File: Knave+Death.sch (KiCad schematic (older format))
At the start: 42 parts, among them J1 OUT0_3.5mm, J2 OUT1_3.5mm, J3 OUT2_3.5mm, J4 PWR_IN_PHNX, J5 OUT3_3.5mm, J6 E0_3.5mm, J7 E1_3.5mm, SW1 SW_SPDT, U1 LM324, U2 LM358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

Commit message: commit before changing schematic
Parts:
- added J8: E1_3.5mm, HammerheadAudio:EuroJack_MonoSW_THT, symbol Connector:Conn_01x03_Male
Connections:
- net GND: now also J8.2 (Pin_2)
- net at U4.14 (CLK): now also J8.1 (Pin_1); no longer U5.3 (Q)
- new net: J8.3 (Pin_3), U5.3 (Q)
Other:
- moved on the sheet: C2, R14, R15, RV1, U5
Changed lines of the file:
@@
 L Timer:NE555 U5
 U 1 1 5E794E13
-P 5100 5300
-F 0 "U5" H 4800 5650 50  0000 C CNN
-F 1 "NE555" H 5350 5650 50  0000 C CNN
-F 2 "Package_DIP:DIP-8_W7.62mm_Socket" H 5100 5300 50  0001 C CNN
-F 3 "http://www.ti.com/lit/ds/symlink/ne555.pdf" H 5100 5300 50  0001 C CNN
-	1    5100 5300
-	1    0    0    -1
-$EndComp
-Wire Wire Line
-	5600 5100 6400 5100
+P 4600 5300
+F 0 "U5" H 4300 5650 50  0000 C CNN
+F 1 "NE555" H 4850 5650 50  0000 C CNN
+F 2 "Package_DIP:DIP-8_W7.62mm_Socket" H 4600 5300 50  0001 C CNN
+F 3 "http://www.ti.com/lit/ds/symlink/ne555.pdf" H 4600 5300 50  0001 C CNN
+	1    4600 5300
+	1    0    0    -1
+$EndComp
 $Comp
 L power:VCC #PWR026
 U 1 1 5E7974FB
-P 4400 5500
-F 0 "#PWR026" H 4400 5350 50  0001 C CNN
-F 1 "VCC" H 4417 5673 50  0000 C CNN
-F 2 "" H 4400 5500 50  0001 C CNN
-F 3 "" H 4400 5500 50  0001 C CNN
-	1    4400 5500
-	1    0    0    -1
-$EndComp
-NoConn ~ 4600 5300
-Wire Wire Line
-	4600 5500 4400 5500
+P 3900 5500
+F 0 "#PWR026" H 3900 5350 50  0001 C CNN
+F 1 "VCC" H 3917 5673 50  0000 C CNN
+F 2 "" H 3900 5500 50  0001 C CNN
+F 3 "" H 3900 5500 50  0001 C CNN
+	1    3900 5500
+	1    0    0    -1
+$EndComp
+NoConn ~ 4100 5300
+Wire Wire Line
+	4100 5500 3900 5500
 $Comp
 L power:GND #PWR028
 U 1 1 5E798069
-P 5100 5750
-F 0 "#PWR028" H 5100 5500 50  0001 C CNN
-F 1 "GND" H 5105 5577 50  0000 C CNN
-F 2 "" H 5100 5750 50  0001 C CNN
-F 3 "" H 5100 5750 50  0001 C CNN
-	1    5100 5750
-	1    0    0    -1
-$EndComp
-Wire Wire Line
-	5100 5750 5100 5700
+P 4600 5750
+F 0 "#PWR028" H 4600 5500 50  0001 C CNN
+F 1 "GND" H 4605 5577 50  0000 C CNN
+F 2 "" H 4600 5750 50  0001 C CNN
+F 3 "" H 4600 5750 50  0001 C CNN
+	1    4600 5750
+	1    0    0    -1
+$EndComp
+Wire Wire Line
+	4600 5750 4600 5700
 $Comp
 L Device:R R15
 U 1 1 5E7988F4
-P 5800 5500
-F 0 "R15" H 5870 5546 50  0000 L CNN
-F 1 "1k" H 5870 5455 50  0000 L CNN
-F 2 "HammerheadAudio:R_THT_P7.62" V 5730 5500 50  0001 C CNN
-F 3 "~" H 5800 5500 50  0001 C CNN
-	1    5800 5500
+P 5300 5500
+F 0 "R15" H 5370 5546 50  0000 L CNN
+F 1 "1k" H 5370 5455 50  0000 L CNN
+F 2 "HammerheadAudio:R_THT_P7.62" V 5230 5500 50  0001 C CNN
+F 3 "~" H 5300 5500 50  0001 C CNN
+	1    5300 5500
 	-1   0    0    1
 $EndComp
@@
 L Device:R R14
 U 1 1 5E799458
-P 5800 4850
-F 0 "R14" H 5870 4896 50  0000 L CNN
-F 1 "1k" H 5870 4805 50  0000 L CNN
-F 2 "HammerheadAudio:R_THT_P7.62" V 5730 4850 50  0001 C CNN
-F 3 "~" H 5800 4850 50  0001 C CNN
-	1    5800 4850
+P 5300 4850
+F 0 "R14" H 5370 4896 50  0000 L CNN
+F 1 "1k" H 5370 4805 50  0000 L CNN
+F 2 "HammerheadAudio:R_THT_P7.62" V 5230 4850 50  0001 C CNN
+F 3 "~" H 5300 4850 50  0001 C CNN
+	1    5300 4850
 	-1   0    0    1
 $EndComp
 Wire Wire Line
-	5800 5350 5800 5300
-Wire Wire Line
-	5800 5000 5800 5300
-Connection ~ 5800 5300
-Wire Wire Line
-	5100 4900 5100 4650
+	5300 5350 5300 5300
+Wire Wire Line
+	5300 5000 5300 5300
+Connection ~ 5300 5300
+Wire Wire Line
+	4600 4900 4600 4650
 $Comp
 L power:VCC #PWR022
 U 1 1 5E79A9DD
-P 5100 4600
-F 0 "#PWR022" H 5100 4450 50  0001 C CNN
-F 1 "VCC" H 5117 4773 50  0000 C CNN
-F 2 "" H 5100 4600 50  0001 C CNN
-F 3 "" H 5100 4600 50  0001 C CNN
-	1    5100 4600
-	1    0    0    -1
-$EndComp
-Wire Wire Line
-	5100 4650 5100 4600
-Connection ~ 5100 4650
+P 4600 4600
+F 0 "#PWR022" H 4600 4450 50  0001 C CNN
+F 1 "VCC" H 4617 4773 50  0000 C CNN
+F 2 "" H 4600 4600 50  0001 C CNN
+F 3 "" H 4600 4600 50  0001 C CNN
+	1    4600 4600
+	1    0    0    -1
+$EndComp
+Wire Wire Line
+	4600 4650 4600 4600
+Connection ~ 4600 4650
 $Comp
 L Device:R_POT_TRIM RV1
 U 1 1 5E79B5EB
-P 5800 5850
-F 0 "RV1" H 5730 5804 50  0000 R CNN
-F 1 "1M" H 5730 5895 50  0000 R CNN
-F 2 "Potentiometer_THT:Potentiometer_Piher_PT-6-V_Vertical" H 5800 5850 50  0001 C CNN
-F 3 "~" H 5800 5850 50  0001 C CNN
-	1    5800 5850
+P 5300 5850
+F 0 "RV1" H 5230 5804 50  0000 R CNN
+F 1 "1M" H 5230 5895 50  0000 R CNN
+F 2 "Potentiometer_THT:Potentiometer_Piher_PT-6-V_Vertical" H 5300 5850 50  0001 C CNN
+F 3 "~" H 5300 5850 50  0001 C CNN
+	1    5300 5850
 	-1   0    0    1
 $EndComp
 Wire Wire Line
-	5800 5700 5800 5650
-Wire Wire Line
-	5800 4650 5800 4700
-Wire Wire Line
-	5100 4650 5800 4650
-Wire Wire Line
-	5600 5300 5800 5300
-Wire Wire Line
-	5600 5500 5600 5850
-Wire Wire Line
-	5600 6050 4300 6050
-Wire Wire Line
-	4300 6050 4300 5100
-Wire Wire Line
-	4300 5100 4600 5100
-Wire Wire Line
-	5600 5850 5650 5850
-Connection ~ 5600 5850
-Wire Wire Line
-	5600 5850 5600 6050
-Wire Wire Line
-	5800 6000 5800 6050
-Wire Wire Line
-	5800 6050 5600 6050
-Connection ~ 5600 6050
+	5300 5700 5300 5650
+Wire Wire Line
+	5300 4650 5300 4700
+Wire Wire Line
+	4600 4650 5300 4650
+Wire Wire Line
+	5100 5300 5300 5300
+Wire Wire Line
+	5100 5500 5100 5850
+Wire Wire Line
+	5100 6050 3800 6050
+Wire Wire Line
+	3800 6050 3800 5100
+Wire Wire Line
+	3800 5100 4100 5100
+Wire Wire Line
+	5100 5850 5150 5850
+Connection ~ 5100 5850
+Wire Wire Line
+	5100 5850 5100 6050
+Wire Wire Line
+	5300 6000 5300 6050
+Wire Wire Line
+	5300 6050 5100 6050
+Connection ~ 5100 6050
 NoConn ~ 7200 5100
 NoConn ~ 7200 5200
@@
 L Device:CP C2
 U 1 1 5E7A1F2F
-P 4300 6250
-F 0 "C2" H 4418 6296 50  0000 L CNN
-F 1 "CP" H 4418 6205 50  0000 L CNN
-F 2 "Capacitor_THT:CP_Radial_D6.3mm_P2.50mm" H 4338 6100 50  0001 C CNN
-F 3 "~" H 4300 6250 50  0001 C CNN
-	1    4300 6250
+P 3800 6250
+F 0 "C2" H 3918 6296 50  0000 L CNN
+F 1 "CP" H 3918 6205 50  0000 L CNN
+F 2 "Capacitor_THT:CP_Radial_D6.3mm_P2.50mm" H 3838 6100 50  0001 C CNN
+F 3 "~" H 3800 6250 50  0001 C CNN
+	1    3800 6250
 	1    0    0    -1
 $EndComp
@@
 L power:GND #PWR029
 U 1 1 5E7A2621
-P 4300 6450
-F 0 "#PWR029" H 4300 6200 50  0001 C CNN
-F 1 "GND" H 4305 6277 50  0000 C CNN
-F 2 "" H 4300 6450 50  0001 C CNN
-F 3 "" H 4300 6450 50  0001 C CNN
-	1    4300 6450
-	1    0    0    -1
-$EndComp
-Wire Wire Line
-	4300 6100 4300 6050
-Connection ~ 4300 6050
-Wire Wire Line
-	4300 6450 4300 6400
+P 3800 6450
+F 0 "#PWR029" H 3800 6200 50  0001 C CNN
+F 1 "GND" H 3805 6277 50  0000 C CNN
+F 2 "" H 3800 6450 50  0001 C CNN
+F 3 "" H 3800 6450 50  0001 C CNN
+	1    3800 6450
+	1    0    0    -1
+$EndComp
+Wire Wire Line
+	3800 6100 3800 6050
+Connection ~ 3800 6050
+Wire Wire Line
+	3800 6450 3800 6400
 $Comp
 L SparkFun-IC-Logic:CD4017 U3
@@
 Wire Wire Line
 	8500 5050 8550 5050
+$Comp
+L Connector:Conn_01x03_Male J8
+U 1 1 5E7ABC41
+P 6050 4450
+F 0 "J8" H 6158 4731 50  0000 C CNN
+F 1 "E1_3.5mm" H 6158 4640 50  0000 C CNN
+F 2 "HammerheadAudio:EuroJack_MonoSW_THT" H 6050 4450 50  0001 C CNN
+F 3 "~" H 6050 4450 50  0001 C CNN
+	1    6050 4450
+	0    1    1    0
+$EndComp
+Wire Wire Line
+	6050 4650 6050 4750
+$Comp
+L power:GND #PWR0101
+U 1 1 5E7ABC4D
+P 6050 4750
+F 0 "#PWR0101" H 6050 4500 50  0001 C CNN
+F 1 "GND" V 6055 4622 50  0000 R CNN
+F 2 "" H 6050 4750 50  0001 C CNN
+F 3 "" H 6050 4750 50  0001 C CNN
+	1    6050 4750
+	1    0    0    -1
+$EndComp
+Wire Wire Line
+	6150 4650 6150 5100
+Wire Wire Line
+	6150 5100 6400 5100
+Wire Wire Line
+	5950 4650 5950 5100
+Wire Wire Line
+	5100 5100 5950 5100
 $EndSCHEMATC

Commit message: updated schematic
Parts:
- added C3: 10uf, Capacitor_THT:CP_Radial_D6.3mm_P2.50mm, symbol Device:CP
- added D9: LED, LED_THT:LED_D5.0mm, symbol Device:LED
- added R16, R18, R19: 1k, HammerheadAudio:R_THT_P7.62, symbol Device:R
- added R17: 220, HammerheadAudio:R_THT_P7.62, symbol Device:R
- added unit 3 of U2
- added unit 4 of U2
- C2: value CP -> 10uf
- R10, R12, R14, R15, R2, R4, R6, R8: value 1k -> 220
- RV1: value 1M -> 100k
- U2: value LM358 -> LM324; footprint Package_DIP:DIP-8_W7.62mm_Socket -> Package_DIP:DIP-14_W7.62mm_Socket; symbol Amplifier_Operational:LM358 -> Amplifier_Operational:LM324
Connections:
- net GND: now also U2.11 (V-), C3.2, D9.1 (K), R19.1; no longer U2.4 (V-)
- net OUT0: no longer U1.2 (-)
- net VCC: now also U2.4 (V+), R18.2; no longer U2.8 (V+)
- net TRIG_IN: now reaches J8.1 (Pin_1)
- net TRIG_IN: now also U2.10 (+); no longer U4.14 (CLK)
- net at C2.1, RV1.1, RV1.2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: now also C3.1
- net at R3.2, R4.2, U1.7: no longer U1.6 (-)
- net at R7.2, R8.2, U1.14: no longer U1.13 (-)
- net at R10.2, R9.2, U2.1: no longer U2.2 (-)
- net at R11.2, R12.2, U2.7: no longer U2.6 (-)
- new net: R16.2, R17.2, U2.8
- new net: D9.2 (A), R17.1
- new net: R18.1, R19.2, U2.12 (+)
- new net TRIG_OUT: R16.1, U4.14 (CLK)
- new net VREF: U1.13 (-), U1.2 (-), U1.6 (-), U2.13 (-), U2.14, U2.2 (-), U2.6 (-), U2.9 (-)
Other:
- moved on the sheet: D0, D1, D2, D3, D4, D5, J1, J2, J3, J5, J6, J7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

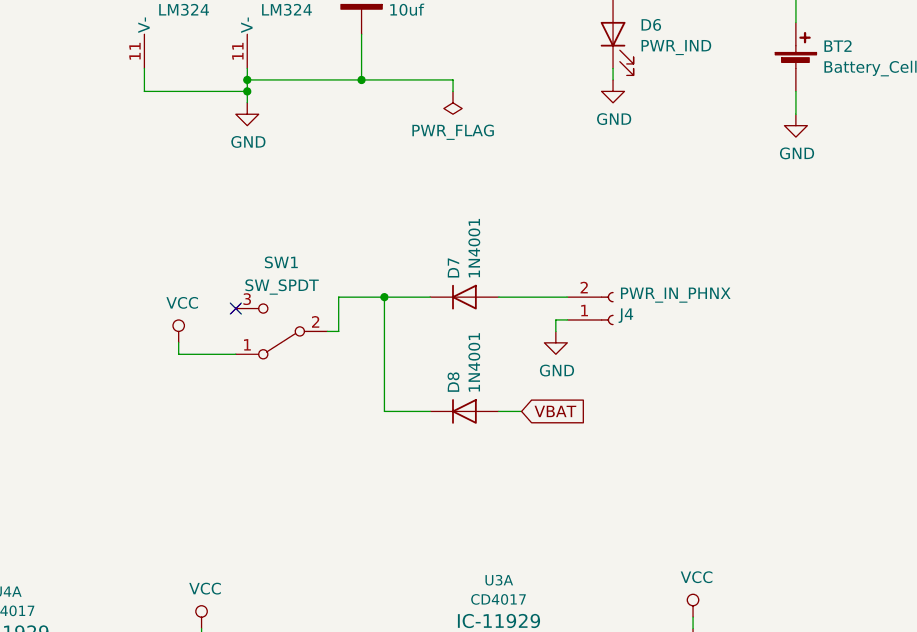
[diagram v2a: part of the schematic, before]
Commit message: removed floral border
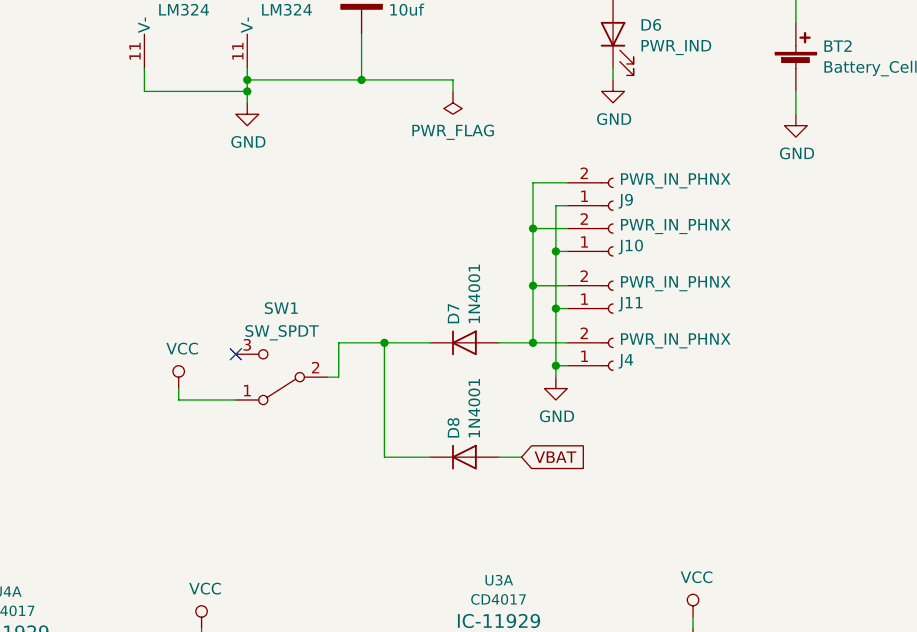
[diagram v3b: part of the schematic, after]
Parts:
- added J10, J11, J9: PWR_IN_PHNX, Connector_Phoenix_MC:PhoenixContact_MC_1,5_2-G-3.81_1x02_P3.81mm_Horizontal, symbol Connector:Conn_01x02_Female
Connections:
- net GND: now also J10.1 (Pin_1), J11.1 (Pin_1), J9.1 (Pin_1)
- net at D7.2 (A), J4.2 (Pin_2): now also J10.2 (Pin_2), J11.2 (Pin_2), J9.2 (Pin_2)
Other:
- moved on the sheet: D7, D8, J4, SW1

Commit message: again...
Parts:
- J10, J11, J4, J9: footprint Connector_Phoenix_MC:PhoenixContact_MC_1,5_2-G-3.81_1x02_P3.81mm_Horizontal -> Connector_Phoenix_MC:PhoenixContact_MCV_1,5_2-G-3.81_1x02_P3.81mm_Vertical
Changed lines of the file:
@@
 F 0 "J4" H 9478 3226 50  0000 L CNN
 F 1 "PWR_IN_PHNX" H 9478 3135 50  0000 L CNN
-F 2 "Connector_Phoenix_MC:PhoenixContact_MC_1,5_2-G-3.81_1x02_P3.81mm_Horizontal" H 9450 3250 50  0001 C CNN
+F 2 "Connector_Phoenix_MC:PhoenixContact_MCV_1,5_2-G-3.81_1x02_P3.81mm_Vertical" H 9450 3250 50  0001 C CNN
 F 3 "~" H 9450 3250 50  0001 C CNN
 	1    9450 3250
@@
 F 0 "J11" H 9478 2976 50  0000 L CNN
 F 1 "PWR_IN_PHNX" H 9478 2885 50  0000 L CNN
-F 2 "Connector_Phoenix_MC:PhoenixContact_MC_1,5_2-G-3.81_1x02_P3.81mm_Horizontal" H 9450 3000 50  0001 C CNN
+F 2 "Connector_Phoenix_MC:PhoenixContact_MCV_1,5_2-G-3.81_1x02_P3.81mm_Vertical" H 9450 3000 50  0001 C CNN
 F 3 "~" H 9450 3000 50  0001 C CNN
 	1    9450 3000
@@
 F 0 "J10" H 9478 2726 50  0000 L CNN
 F 1 "PWR_IN_PHNX" H 9478 2635 50  0000 L CNN
-F 2 "Connector_Phoenix_MC:PhoenixContact_MC_1,5_2-G-3.81_1x02_P3.81mm_Horizontal" H 9450 2750 50  0001 C CNN
+F 2 "Connector_Phoenix_MC:PhoenixContact_MCV_1,5_2-G-3.81_1x02_P3.81mm_Vertical" H 9450 2750 50  0001 C CNN
 F 3 "~" H 9450 2750 50  0001 C CNN
 	1    9450 2750
@@
 F 0 "J9" H 9478 2526 50  0000 L CNN
 F 1 "PWR_IN_PHNX" H 9478 2435 50  0000 L CNN
-F 2 "Connector_Phoenix_MC:PhoenixContact_MC_1,5_2-G-3.81_1x02_P3.81mm_Horizontal" H 9450 2550 50  0001 C CNN
+F 2 "Connector_Phoenix_MC:PhoenixContact_MCV_1,5_2-G-3.81_1x02_P3.81mm_Vertical" H 9450 2550 50  0001 C CNN
 F 3 "~" H 9450 2550 50  0001 C CNN
 	1    9450 2550

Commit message: most traces
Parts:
- removed R16: 1k, HammerheadAudio:R_THT_P7.62, symbol Device:R
- renumbered R17 to R16, R18 to R17, R19 to R18
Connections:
- net TRIG_OUT: now also R16.2, U2.8
- net VREF: now also U1.9 (-)
- net at R5.2, R6.2, U1.8: no longer U1.9 (-)
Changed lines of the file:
@@
 $EndComp
-Wire Wire Line
-	1000 2750 1000 2950
-Wire Wire Line
-	1000 2950 1650 2950
-Wire Wire Line
-	1650 2950 1650 2650
 Wire Wire Line
 	1650 2650 1600 2650
@@
 	1    0    0    -1
 $EndComp
-Wire Wire Line
-	1650 2950 1650 3000
-Connection ~ 1650 2950
 Connection ~ 1650 2650
 Wire Wire Line
@@
 $Comp
 L Device:R R16
-U 1 1 5E7C45DB
-P 1900 6200
-F 0 "R16" V 1693 6200 50  0000 C CNN
-F 1 "1k" V 1784 6200 50  0000 C CNN
-F 2 "HammerheadAudio:R_THT_P7.62" V 1830 6200 50  0001 C CNN
-F 3 "~" H 1900 6200 50  0001 C CNN
-	1    1900 6200
-	0    1    1    0
-$EndComp
-$Comp
-L Device:R R17
 U 1 1 5E7C45E5
 P 1900 6550
-F 0 "R17" V 1693 6550 50  0000 C CNN
+F 0 "R16" V 1693 6550 50  0000 C CNN
 F 1 "220" V 1784 6550 50  0000 C CNN
 F 2 "HammerheadAudio:R_THT_P7.62" V 1830 6550 50  0001 C CNN
@@
 	950  6100 1000 6100
 Wire Wire Line
-	1650 6200 1750 6200
-Wire Wire Line
 	1650 6550 1750 6550
 $Comp
@@
 	1650 7250 1750 7250
 $Comp
-L Device:R R19
+L Device:R R18
 U 1 1 5E8114BF
 P 700 7350
-F 0 "R19" V 493 7350 50  0000 C CNN
+F 0 "R18" V 493 7350 50  0000 C CNN
 F 1 "1k" V 584 7350 50  0000 C CNN
 F 2 "HammerheadAudio:R_THT_P7.62" V 630 7350 50  0001 C CNN
@@
 $EndComp
 $Comp
-L Device:R R18
+L Device:R R17
 U 1 1 5E81215C
 P 700 6950
-F 0 "R18" V 493 6950 50  0000 C CNN
+F 0 "R17" V 493 6950 50  0000 C CNN
 F 1 "1k" V 584 6950 50  0000 C CNN
 F 2 "HammerheadAudio:R_THT_P7.62" V 630 6950 50  0001 C CNN
@@
 Wire Wire Line
 	700  7150 700  7200
-Wire Wire Line
-	2050 6200 2400 6200
 Wire Wire Line
 	1650 4450 1650 4800
@@
 Wire Wire Line
 	9100 2900 9100 3150
+Wire Wire Line
+	1650 2650 1650 3000
+Wire Wire Line
+	950  2750 1000 2750
+Wire Wire Line
+	1650 6200 2400 6200
 $EndSCHEMATC

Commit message: finished layout
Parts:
- C1, C2, C3: footprint Capacitor_THT:CP_Radial_D6.3mm_P2.50mm -> Capacitor_THT:CP_Radial_D5.0mm_P2.00mm
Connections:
- net TT0 is gone; now on net FF0: U2.3 (+)
- net TT1 is gone; now on net FF1: U2.5 (+)
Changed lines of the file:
@@
 F 0 "C2" H 3918 6296 50  0000 L CNN
 F 1 "10uf" H 3918 6205 50  0000 L CNN
-F 2 "Capacitor_THT:CP_Radial_D6.3mm_P2.50mm" H 3838 6100 50  0001 C CNN
+F 2 "Capacitor_THT:CP_Radial_D5.0mm_P2.00mm" H 3838 6100 50  0001 C CNN
 F 3 "~" H 3800 6250 50  0001 C CNN
 	1    3800 6250
@@
 	2450 4800 2400 4800
 Text GLabel 950  4350 0    50   Input ~ 0
-TT0
+FF0
 Wire Wire Line
 	950  4350 1000 4350
@@
 	2450 5650 2400 5650
 Text GLabel 950  5200 0    50   Input ~ 0
-TT1
+FF1
 Wire Wire Line
 	950  5200 1000 5200
@@
 F 0 "C1" H 8468 1696 50  0000 L CNN
 F 1 "10uf" H 8468 1605 50  0000 L CNN
-F 2 "Capacitor_THT:CP_Radial_D6.3mm_P2.50mm" H 8388 1500 50  0001 C CNN
+F 2 "Capacitor_THT:CP_Radial_D5.0mm_P2.00mm" H 8388 1500 50  0001 C CNN
 F 3 "~" H 8350 1650 50  0001 C CNN
 	1    8350 1650
@@
 F 0 "C3" H 4318 6296 50  0000 L CNN
 F 1 "10uf" H 4318 6205 50  0000 L CNN
-F 2 "Capacitor_THT:CP_Radial_D6.3mm_P2.50mm" H 4238 6100 50  0001 C CNN
+F 2 "Capacitor_THT:CP_Radial_D5.0mm_P2.00mm" H 4238 6100 50  0001 C CNN
 F 3 "~" H 4200 6250 50  0001 C CNN
 	1    4200 6250
